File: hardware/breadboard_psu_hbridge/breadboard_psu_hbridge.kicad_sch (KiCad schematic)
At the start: 49 parts, among them J1 USB_B_Micro, J2 Conn_01x02, J3 Conn_01x02, U1 74LS132, U2 LM4871MX_NOPB, U3 LM2733YMF, U4 ZXBM5210-S

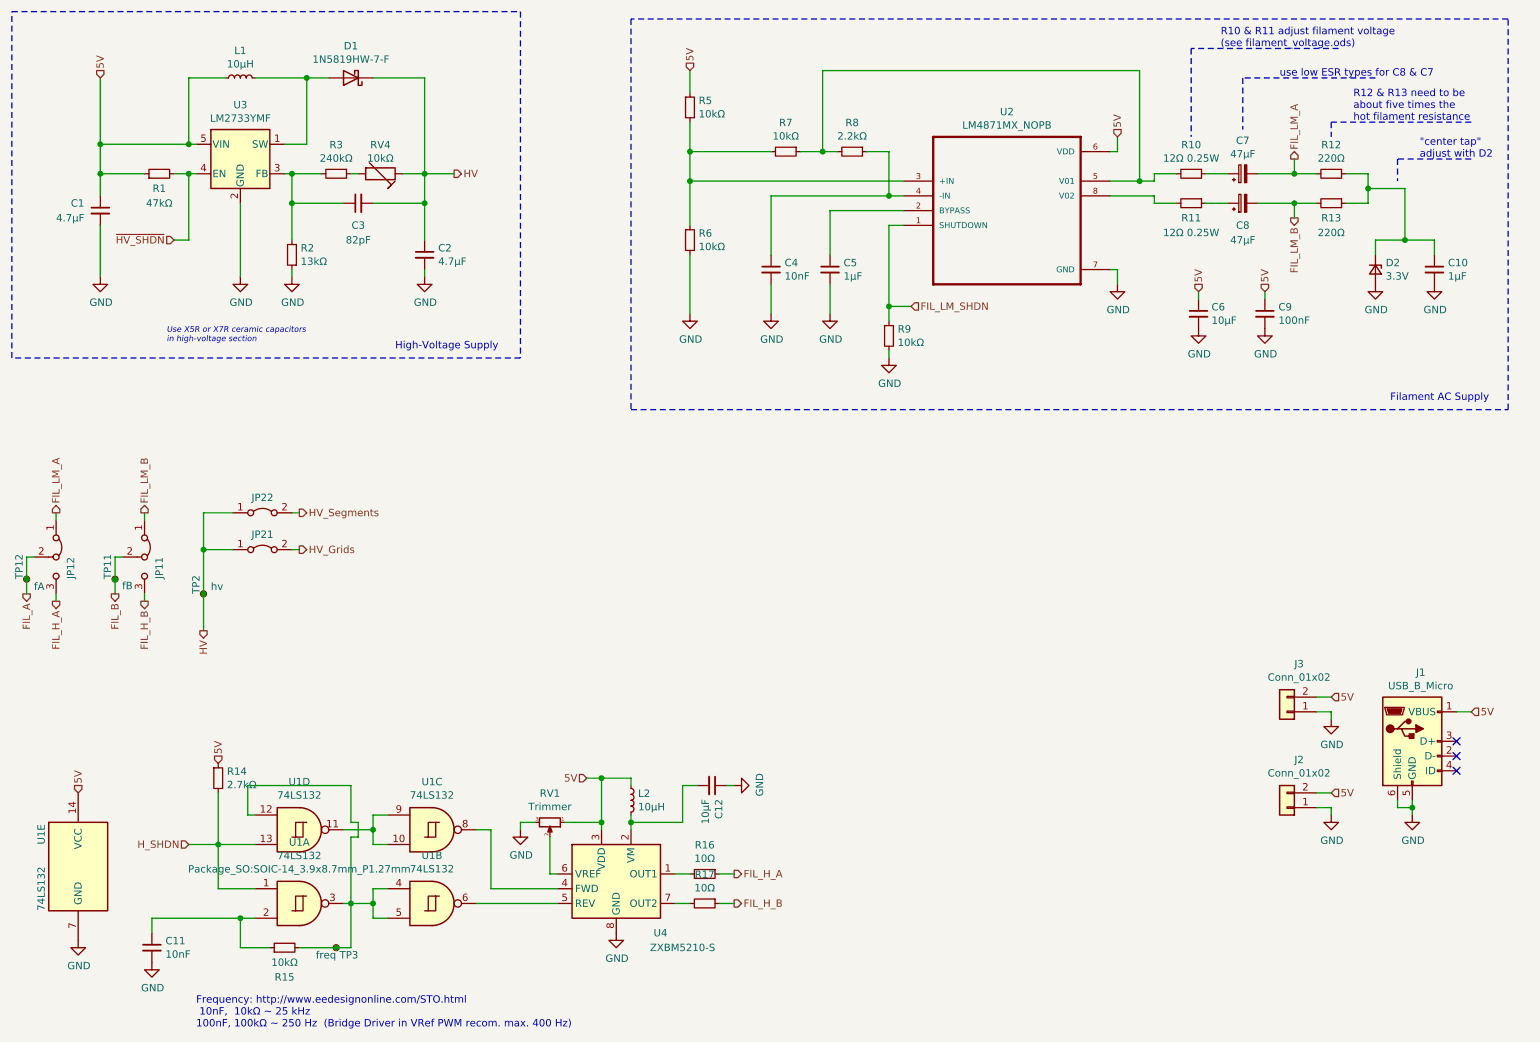
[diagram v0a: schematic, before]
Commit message: hw: finished h-bridge psu test board
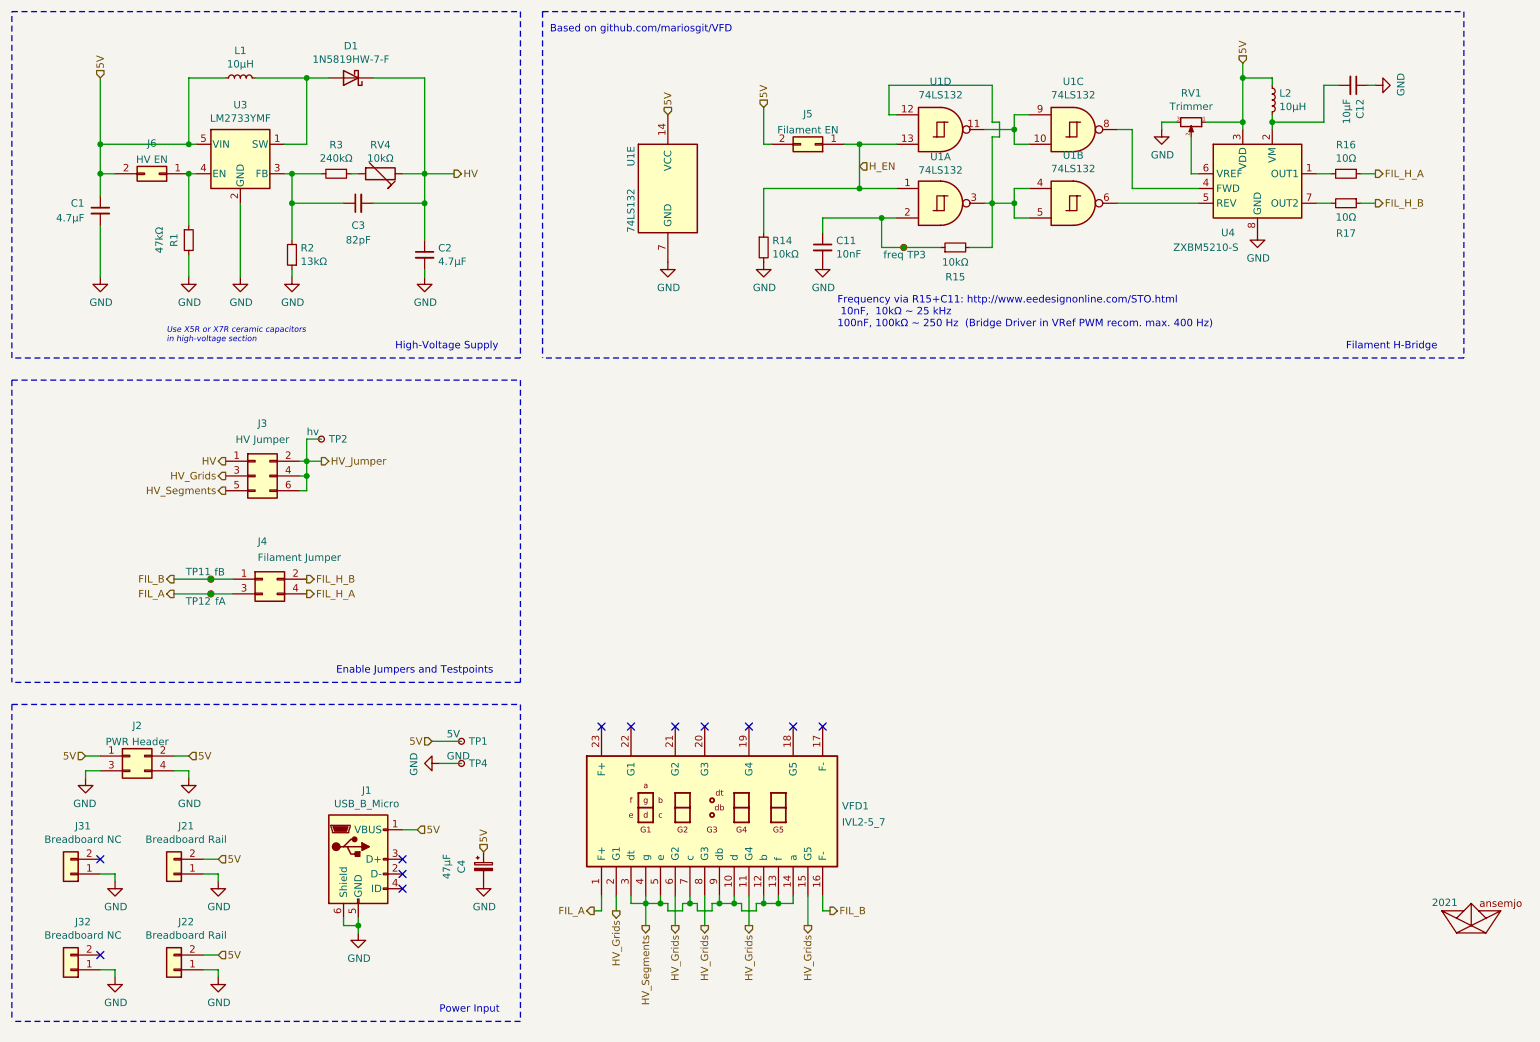
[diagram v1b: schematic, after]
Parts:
- removed C10, C5: 1µF, Capacitor_SMD:C_0805_2012Metric_Pad1.15x1.40mm_HandSolder, symbol Device:C_Small
- removed C4: 10nF, Capacitor_SMD:C_0805_2012Metric_Pad1.15x1.40mm_HandSolder, symbol Device:C_Small
- removed C6: 10µF, Capacitor_SMD:C_0805_2012Metric_Pad1.18x1.45mm_HandSolder, symbol Device:C_Small
- removed C7, C8: 47µF, Capacitor_SMD:CP_Elec_6.3x5.9, symbol Device:CP_Small
- removed C9: 100nF, Capacitor_SMD:C_0805_2012Metric_Pad1.15x1.40mm_HandSolder, symbol Device:C_Small
- removed D2: 3.3V, Diode_SMD:D_SOD-123, symbol Device:D_Zener_Small
- removed JP11, JP12: Jumper_3_Bridged12, Connector_PinHeader_2.54mm:PinHeader_1x03_P2.54mm_Vertical, symbol Jumper:Jumper_3_Bridged12
- removed JP21, JP22: Jumper_2_Bridged, Connector_PinHeader_2.54mm:PinHeader_1x02_P2.54mm_Vertical, symbol Jumper:Jumper_2_Bridged
- removed R10, R11: 12Ω 0.25W, Resistor_SMD:R_1206_3216Metric_Pad1.42x1.75mm_HandSolder, symbol Device:R_Small
- removed R12, R13: 220Ω, Resistor_SMD:R_0805_2012Metric_Pad1.15x1.40mm_HandSolder, symbol Device:R_Small
- removed R5, R6, R7, R9: 10kΩ, Resistor_SMD:R_0805_2012Metric_Pad1.15x1.40mm_HandSolder, symbol Device:R_Small
- removed R8: 2.2kΩ, Resistor_SMD:R_0805_2012Metric_Pad1.15x1.40mm_HandSolder, symbol Device:R_Small
- removed U2: LM4871MX_NOPB, Package_SO:SOIC-8_3.9x4.9mm_P1.27mm, symbol breadboard_psu_hbridge-rescue:LM4871MX_NOPB-LM4871MX_NOPB
- added A1: 2021, extra:AHOI, symbol ahoi:ahoi
- added C4: 47µF, Capacitor_SMD:CP_Elec_6.3x5.9, symbol Device:CP_Small
- added J2: PWR Header, Connector_PinHeader_2.54mm:PinHeader_2x02_P2.54mm_Vertical, symbol Connector_Generic:Conn_02x02_Odd_Even
- added J3: HV Jumper, Connector_PinHeader_2.54mm:PinHeader_2x03_P2.54mm_Vertical, symbol Connector_Generic:Conn_02x03_Odd_Even
- added J31, J32: Breadboard NC, Connector_PinHeader_2.54mm:PinHeader_1x02_P2.54mm_Vertical, symbol Connector_Generic:Conn_01x02
- added J4: Filament Jumper, Connector_PinHeader_2.54mm:PinHeader_2x02_P2.54mm_Vertical, symbol Connector_Generic:Conn_02x02_Odd_Even
- added J5: Filament EN, Connector_PinHeader_2.54mm:PinHeader_2x01_P2.54mm_Vertical, symbol Connector_Generic:Conn_02x01
- added J6: HV EN, Connector_PinHeader_2.54mm:PinHeader_2x01_P2.54mm_Vertical, symbol Connector_Generic:Conn_02x01
- added TP1: 5V, TestPoint:TestPoint_THTPad_D1.5mm_Drill0.7mm, symbol Connector:TestPoint_Small
- added TP4: GND, TestPoint:TestPoint_THTPad_D1.5mm_Drill0.7mm, symbol Connector:TestPoint_Small
- added VFD1: IVL2-5_7, extra:IVL2-7_5-singleSide, symbol extra:IVL2-5_7
- J21: renamed from J3; value Conn_01x02 -> Breadboard Rail
- J22: renamed from J2; value Conn_01x02 -> Breadboard Rail
- R14: value 2.7kΩ -> 10kΩ
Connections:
- net 5V: now also C4.1, J2.1 (Pin_1), J2.2 (Pin_2), J5.2 (Pin_2), J6.2 (Pin_2), TP1.1; no longer R1.1, R14.1
- net FIL_A: now also J4.3 (Pin_3), VFD1.1 (F+)
- net FIL_B: now also J4.1 (Pin_1), VFD1.16 (F-)
- net FIL_H_A: now also J4.4 (Pin_4)
- net FIL_H_B: now also J4.2 (Pin_2)
- net GND: now also R1.2, R14.2, C4.2, J2.3 (Pin_3), J2.4 (Pin_4), J31.1 (Pin_1), J32.1 (Pin_1), TP4.1
- net HV: now also J3.1 (Pin_1); no longer TP2.1
- net HV_Grids: now also J3.3 (Pin_3), VFD1.11 (G4), VFD1.15 (G5), VFD1.2 (G1), VFD1.6 (G2), VFD1.8 (G3)
- net HV_Segments: now also J3.5 (Pin_5), VFD1.10 (d), VFD1.12 (b), VFD1.13 (f), VFD1.14 (a), VFD1.3 (dt), VFD1.4 (g), VFD1.5 (e), VFD1.7 (c), VFD1.9 (db)
- net at C11.1, R15.1, U1.2: now also TP3.1
- net at R15.2, U1.12, U1.3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: no longer TP3.1
- net H_SHDN renamed H_EN
- net H_EN: now also R14.1, J5.1 (Pin_1); no longer R14.2
- net ~{HV_SHDN}: no longer names the net of U3.4 (EN)
- net ~{HV_SHDN}: now also R1.1, J6.1 (Pin_1); no longer R1.2
- new net HV_Jumper: J3.2 (Pin_2), J3.4 (Pin_4), J3.6 (Pin_6), TP2.1
- no-connect marks 3 -> 12
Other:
- note added: "Based on github.com/mariosgit/VFD"
- note added: "Enable Jumpers and Testpoints"
- note added: "Filament H-Bridge"
- note added: "Frequency via R15+C11: http://www.eedesignonline.com/STO.html 10nF, 10kΩ ~ 25 kHz 100nF, 100kΩ ~ 250 Hz (Bridge Driver in VRef PWM recom. max. 400 Hz)"
- note added: "Power Input"
- note removed: ""center tap" adjust with D2"
- note removed: "Filament AC Supply"
- note removed: "Frequency: http://www.eedesignonline.com/STO.html 10nF, 10kΩ ~ 25 kHz 100nF, 100kΩ ~ 250 Hz (Bridge Driver in VRef PWM recom. max. 400 Hz)"
- note removed: "R10 & R11 adjust filament voltage (see filament_voltage.ods)"
- note removed: "R12 & R13 need to be about five times the hot filament resistance"
- note removed: "use low ESR types for C8 & C7"
- moved on the sheet: C11, C12, J1, J21, J22, L2, R1, R14, R15, R16, R17, RV1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

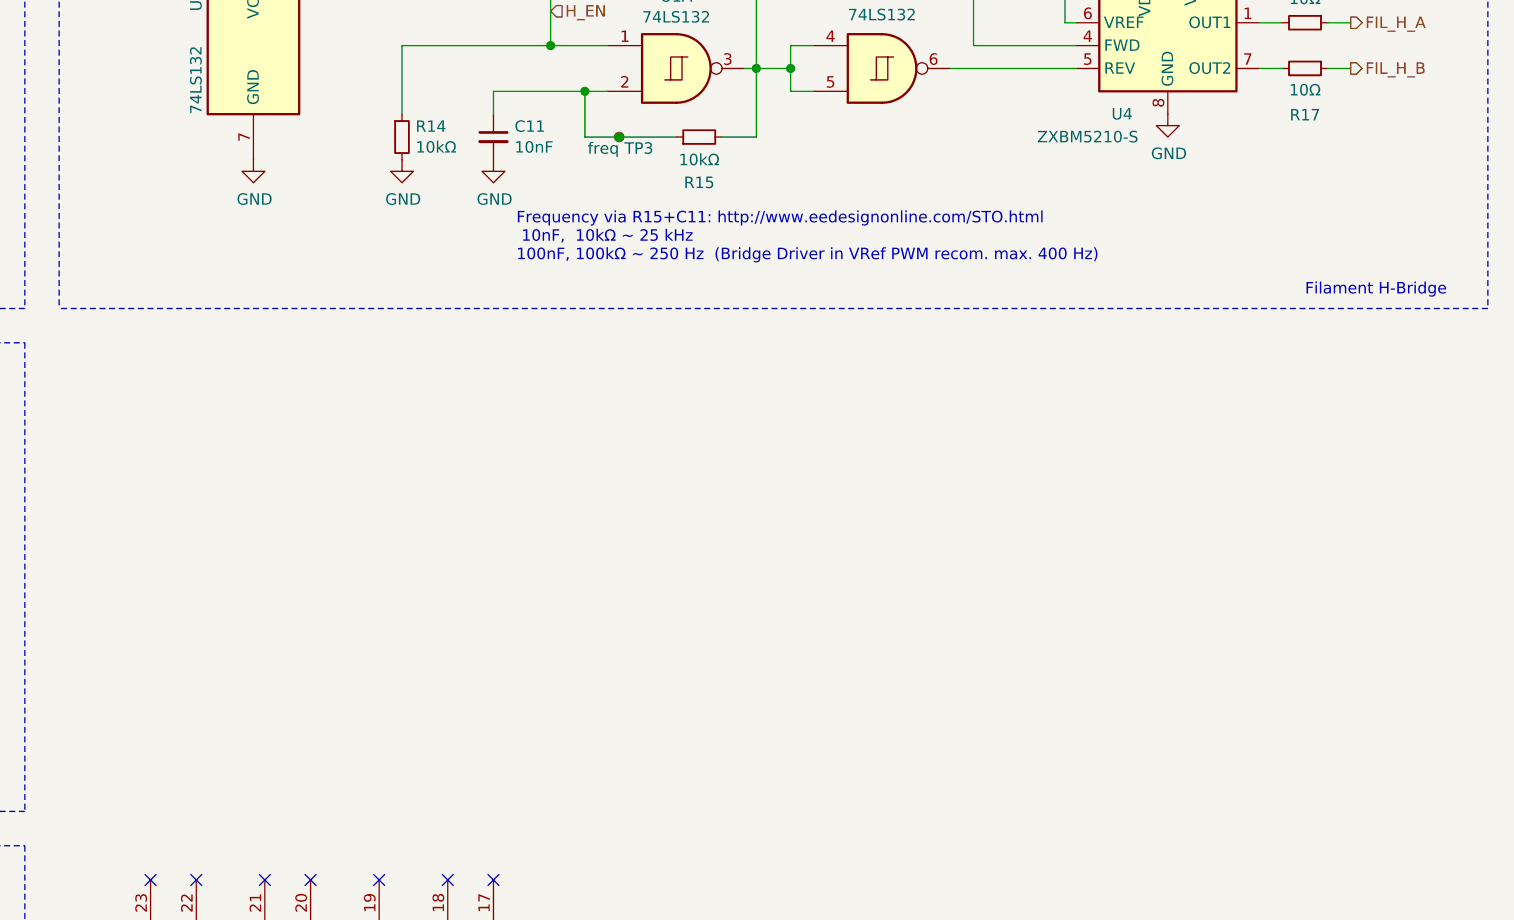
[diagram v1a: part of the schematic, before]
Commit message: hw: update h-bridge psu with experiences as text on schematic
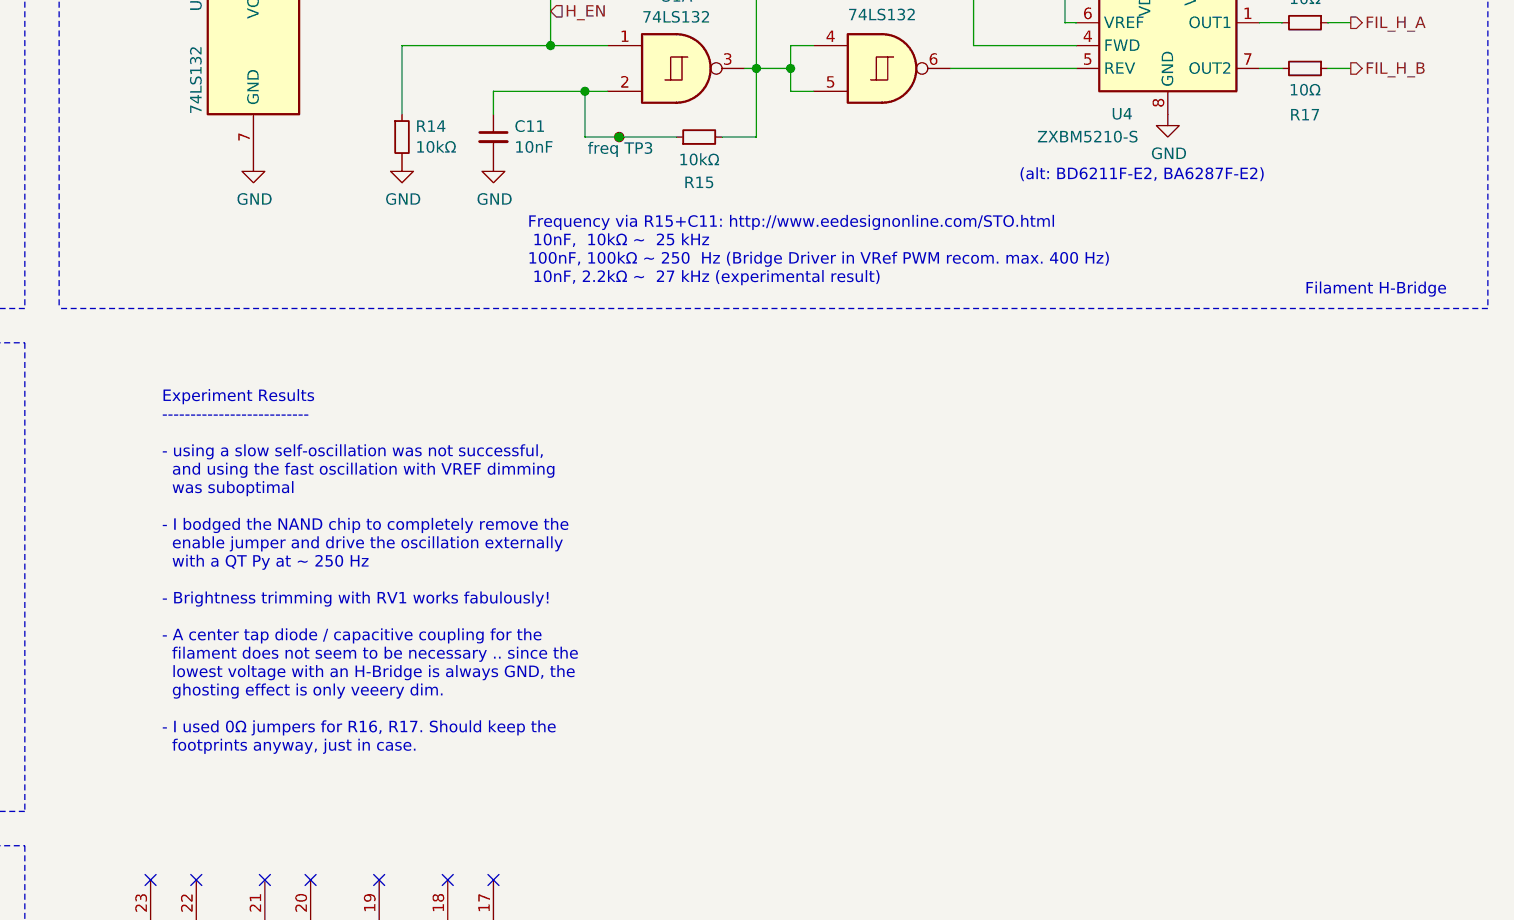
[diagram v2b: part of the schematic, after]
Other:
- note added: "(alt: BD6211F-E2, BA6287F-E2)"
- note added: "Experiment Results -------------------------- - using a slow self-oscillation was not successful, and using the fast oscillation with VREF dimming was suboptimal - I bodged the NAND chip to completely remove the enable jumper and drive the oscillation externally with a QT Py at ~ 250 Hz - Brightness trimming with RV1 works fabulously! - A center tap diode / capacitive coupling for the filament do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"
- note added: "Frequency via R15+C11: http://www.eedesignonline.com/STO.html 10nF, 10kΩ ~ 25 kHz 100nF, 100kΩ ~ 250 Hz (Bridge Driver in VRef PWM recom. max. 400 Hz) 10nF, 2.2kΩ ~ 27 kHz (experimental result)"
- note removed: "Frequency via R15+C11: http://www.eedesignonline.com/STO.html 10nF, 10kΩ ~ 25 kHz 100nF, 100kΩ ~ 250 Hz (Bridge Driver in VRef PWM recom. max. 400 Hz)"
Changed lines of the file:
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@@
     (effects (font (size 1.27 1.27)) (justify left bottom))
   )
-  (text "Frequency via R15+C11: http://www.eedesignonline.com/STO.html\n 10nF,  10kΩ ~ 25 kHz\n100nF, 100kΩ ~ 250 Hz  (Bridge Driver in VRef PWM recom. max. 400 Hz)"
-    (at 161.29 72.39 0)
+  (text "Experiment Results\n--------------------------\n\n- using a slow self-oscillation was not successful,\n  and using the fast oscillation with VREF dimming\n  was suboptimal\n\n- I bodged the NAND chip to completely remove the\n  enable jumper and drive the oscillation externally\n  with a QT Py at ~ 250 Hz\n\n- Brightness trimming with RV1 works fabulously!\n\n- A center tap diode / capacitive coupling for the\n  filament does not seem to be necessary .. since the\n  lowest voltage with an H-Bridge is always GND, the\n  ghosting effect is only veeery dim.\n\n- I used 0Ω jumpers for R16, R17. Should keep the\n  footprints anyway, just in case."
+    (at 121.92 127 0)
+    (effects (font (size 1.27 1.27)) (justify left bottom))
+  )
+  (text "Frequency via R15+C11: http://www.eedesignonline.com/STO.html\n 10nF,  10kΩ ~  25 kHz\n100nF, 100kΩ ~ 250  Hz (Bridge Driver in VRef PWM recom. max. 400 Hz)\n 10nF, 2.2kΩ ~  27 kHz (experimental result)"
+    (at 162.56 74.93 0)
+    (effects (font (size 1.27 1.27)) (justify left bottom))
+  )
+  (text "(alt: BD6211F-E2, BA6287F-E2)" (at 217.17 63.5 0)
     (effects (font (size 1.27 1.27)) (justify left bottom))
   )
@@
     (pin "2")
   )
+  (symbol (lib_id "Device:RTRIM") (at 82.55 45.72 270) (unit 1)
+    (in_bom yes) (on_board yes)
+    (property "Reference" "RV4" (id 0) (at 82.55 40.7416 90))
+    (property "Value" "10kΩ" (id 1) (at 82.55 43.053 90))
+    (property "Footprint" "Potentiometer_THT:Potentiometer_Bourns_3266W_Vertical" (id 2) (at 82.55 45.72 0)
+      (effects (font (size 1.27 1.27)) hide)
+    )
+    (property "Datasheet" "~" (id 3) (at 82.55 45.72 0)
+      (effects (font (size 1.27 1.27)) hide)
+    )
+    (property "Digi-Key PN" "311-10.0KCRCT-ND" (id 4) (at 82.55 45.72 0)
+      (effects (font (size 1.27 1.27)) hide)
+    )
+    (property "MPN" "RC0805FR-0710KL" (id 5) (at 82.55 45.72 0)
+      (effects (font (size 1.27 1.27)) hide)
+    )
+    (property "Mfg" "Yageo" (id 6) (at 82.55 45.72 0)
+      (effects (font (size 1.27 1.27)) hide)
+    )
+    (pin "1")
+    (pin "2")
+  )
   (symbol (lib_id "Connector_Generic:Conn_01x02") (at 29.21 166.37 180) (unit 1)
     (in_bom yes) (on_board yes)
@@
       (effects (font (size 1.27 1.27)) hide)
     )
-    (pin "1")
-    (pin "2")
-  )
-  (symbol (lib_id "Device:RTRIM") (at 82.55 45.72 270) (unit 1)
-    (in_bom yes) (on_board yes)
-    (property "Reference" "RV4" (id 0) (at 82.55 40.7416 90))
-    (property "Value" "10kΩ" (id 1) (at 82.55 43.053 90))
-    (property "Footprint" "Potentiometer_THT:Potentiometer_Bourns_3266W_Vertical" (id 2) (at 82.55 45.72 0)
-      (effects (font (size 1.27 1.27)) hide)
-    )
-    (property "Datasheet" "~" (id 3) (at 82.55 45.72 0)
-      (effects (font (size 1.27 1.27)) hide)
-    )
-    (property "Digi-Key PN" "311-10.0KCRCT-ND" (id 4) (at 82.55 45.72 0)
-      (effects (font (size 1.27 1.27)) hide)
-    )
-    (property "MPN" "RC0805FR-0710KL" (id 5) (at 82.55 45.72 0)
-      (effects (font (size 1.27 1.27)) hide)
-    )
-    (property "Mfg" "Yageo" (id 6) (at 82.55 45.72 0)
-      (effects (font (size 1.27 1.27)) hide)
-    )
